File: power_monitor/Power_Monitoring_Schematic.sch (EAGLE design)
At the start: 15 parts, among them U1 INA3221.

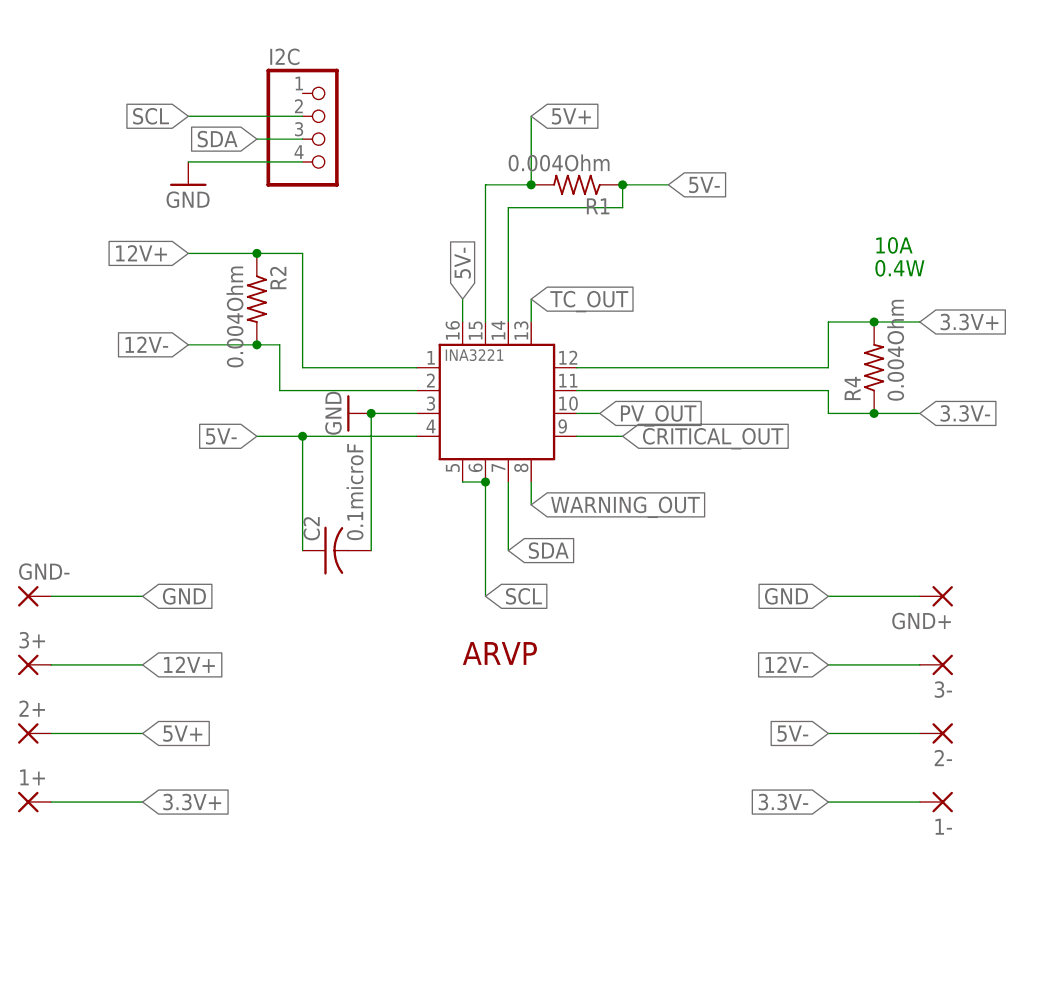
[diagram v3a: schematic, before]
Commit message: Added dedicated power connector and CAM files
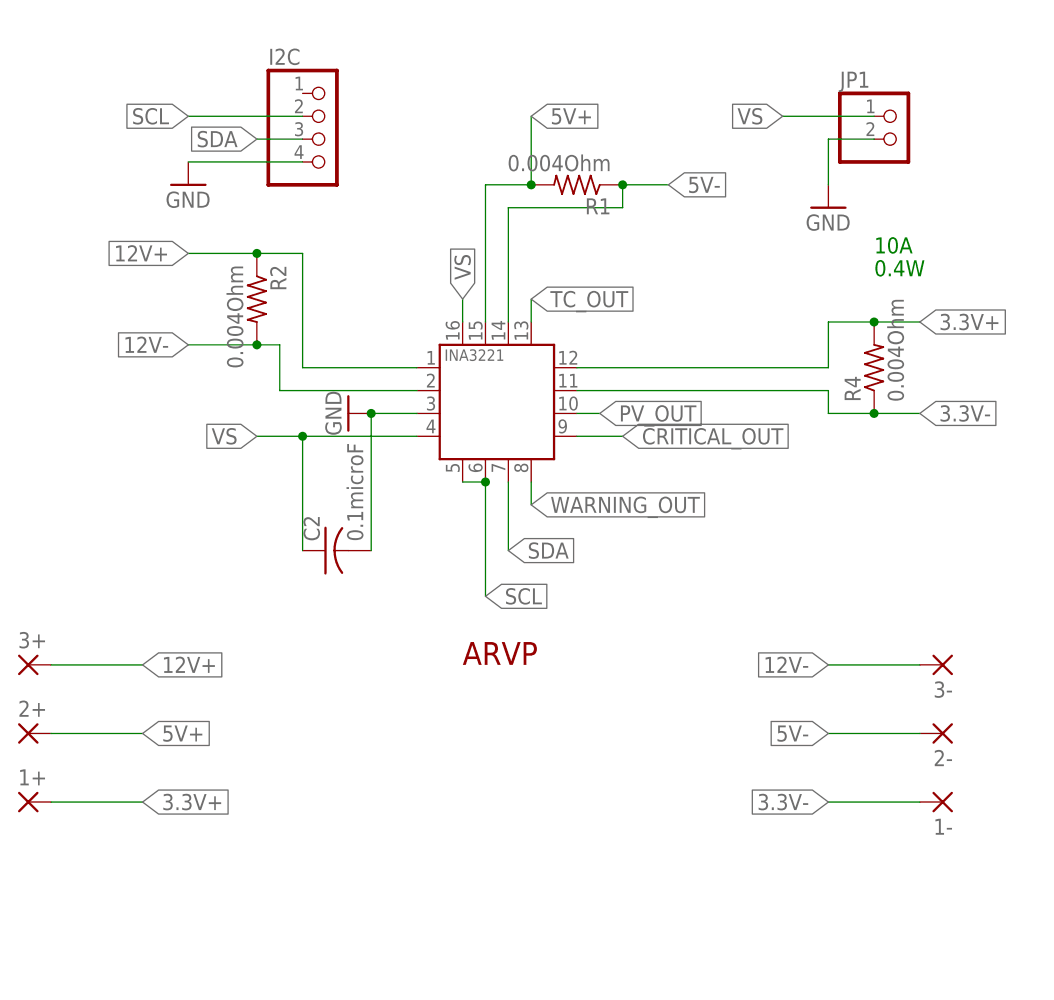
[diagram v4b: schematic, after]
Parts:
- removed GND+, GND-: (no value), Moira:3,81/1,5A
- added JP1: (no value), pinhead:PINHD-1X2
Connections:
- new net VS: C2.1, JP1.1, U1.VPU, U1.VS
- net 5V-: no longer C2.1, U1.VPU, U1.VS
- net GND: now also JP1.2; no longer GND+.P, GND-.P
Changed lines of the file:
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@@
 <part name="I2C" library="pinhead" library_urn="urn:adsk.eagle:library:325" deviceset="PINHD-1X4" device="" package3d_urn="urn:adsk.eagle:package:22407/2"/>
 <part name="GND1" library="supply1" deviceset="GND" device=""/>
-<part name="GND-" library="Moira" deviceset="3,81/1,5" device="A"/>
 <part name="3+" library="Moira" deviceset="3,81/1,5" device="A"/>
 <part name="2+" library="Moira" deviceset="3,81/1,5" device="A"/>
 <part name="1+" library="Moira" deviceset="3,81/1,5" device="A"/>
-<part name="GND+" library="Moira" deviceset="3,81/1,5" device="A"/>
 <part name="3-" library="Moira" deviceset="3,81/1,5" device="A"/>
 <part name="2-" library="Moira" deviceset="3,81/1,5" device="A"/>
 <part name="1-" library="Moira" deviceset="3,81/1,5" device="A"/>
 <part name="ARVP1" library="ARVP" deviceset="ARVP_LOGO" device=""/>
+<part name="JP1" library="pinhead" library_urn="urn:adsk.eagle:library:325" deviceset="PINHD-1X2" device="" package3d_urn="urn:adsk.eagle:package:22435/2"/>
+<part name="GND2" library="supply1" deviceset="GND" device=""/>
 </parts>
 <sheets>
@@
 <instance part="I2C" gate="A" x="-15.24" y="27.94"/>
 <instance part="GND1" gate="1" x="-30.48" y="22.86"/>
-<instance part="GND-" gate="1" x="-48.26" y="-22.86"/>
 <instance part="3+" gate="1" x="-48.26" y="-30.48"/>
 <instance part="2+" gate="1" x="-48.26" y="-38.1"/>
 <instance part="1+" gate="1" x="-48.26" y="-45.72"/>
-<instance part="GND+" gate="1" x="53.34" y="-22.86" rot="R180"/>
 <instance part="3-" gate="1" x="53.34" y="-30.48" rot="R180"/>
 <instance part="2-" gate="1" x="53.34" y="-38.1" rot="R180"/>
 <instance part="1-" gate="1" x="53.34" y="-45.72" rot="R180"/>
 <instance part="ARVP1" gate="G$1" x="2.54" y="-30.48"/>
+<instance part="JP1" gate="G$1" x="48.26" y="27.94"/>
+<instance part="GND2" gate="1" x="40.64" y="20.32"/>
 </instances>
 <busses>
@@
 </segment>
 <segment>
-<pinref part="GND-" gate="1" pin="P"/>
-<wire x1="-45.72" y1="-22.86" x2="-35.56" y2="-22.86" width="0.1524" layer="91"/>
-<label x="-35.56" y="-22.86" size="1.778" layer="95" xref="yes"/>
-</segment>
-<segment>
-<pinref part="GND+" gate="1" pin="P"/>
-<wire x1="50.8" y1="-22.86" x2="40.64" y2="-22.86" width="0.1524" layer="91"/>
-<label x="40.64" y="-22.86" size="1.778" layer="95" rot="R180" xref="yes"/>
+<pinref part="JP1" gate="G$1" pin="2"/>
+<wire x1="45.72" y1="27.94" x2="40.64" y2="27.94" width="0.1524" layer="91"/>
+<wire x1="40.64" y1="27.94" x2="40.64" y2="22.86" width="0.1524" layer="91"/>
+<pinref part="GND2" gate="1" pin="GND"/>
 </segment>
 </net>
@@
 <label x="40.64" y="-38.1" size="1.778" layer="95" rot="R180" xref="yes"/>
 </segment>
-<segment>
-<pinref part="U1" gate="G$1" pin="VS"/>
-<wire x1="-17.78" y1="-5.08" x2="-5.08" y2="-5.08" width="0.1524" layer="91"/>
-<wire x1="-17.78" y1="-17.78" x2="-17.78" y2="-5.08" width="0.1524" layer="91"/>
-<wire x1="-17.78" y1="-5.08" x2="-22.86" y2="-5.08" width="0.1524" layer="91"/>
-<junction x="-17.78" y="-5.08"/>
-<label x="-22.86" y="-5.08" size="1.778" layer="95" rot="R180" xref="yes"/>
-<pinref part="C2" gate="G$1" pin="1"/>
-</segment>
-<segment>
-<pinref part="U1" gate="G$1" pin="VPU"/>
-<wire x1="0" y1="7.62" x2="0" y2="10.16" width="0.1524" layer="91"/>
-<label x="0" y="10.16" size="1.778" layer="95" rot="R90" xref="yes"/>
-</segment>
 </net>
 <net name="SDA" class="0">
@@
 </segment>
 </net>
+<net name="VS" class="0">
+<segment>
+<pinref part="U1" gate="G$1" pin="VPU"/>
+<wire x1="0" y1="7.62" x2="0" y2="10.16" width="0.1524" layer="91"/>
+<label x="0" y="10.16" size="1.778" layer="95" rot="R90" xref="yes"/>
+</segment>
+<segment>
+<pinref part="U1" gate="G$1" pin="VS"/>
+<wire x1="-17.78" y1="-5.08" x2="-5.08" y2="-5.08" width="0.1524" layer="91"/>
+<wire x1="-17.78" y1="-17.78" x2="-17.78" y2="-5.08" width="0.1524" layer="91"/>
+<wire x1="-17.78" y1="-5.08" x2="-22.86" y2="-5.08" width="0.1524" layer="91"/>
+<junction x="-17.78" y="-5.08"/>
+<label x="-22.86" y="-5.08" size="1.778" layer="95" rot="R180" xref="yes"/>
+<pinref part="C2" gate="G$1" pin="1"/>
+</segment>
+<segment>
+<pinref part="JP1" gate="G$1" pin="1"/>
+<wire x1="45.72" y1="30.48" x2="35.56" y2="30.48" width="0.1524" layer="91"/>
+<label x="35.56" y="30.48" size="1.778" layer="95" rot="R180" xref="yes"/>
+</segment>
+</net>
